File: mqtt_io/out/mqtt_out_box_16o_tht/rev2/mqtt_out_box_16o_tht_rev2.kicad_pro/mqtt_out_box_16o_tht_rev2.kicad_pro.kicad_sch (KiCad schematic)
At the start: 146 parts, among them J1 Conn_01x03_Pin, J2 Conn_01x03_Pin, Q1 IRFZ24N, SW1 SW_DIP_x03, U1 MCP23017_SP, U2 LF33_TO220

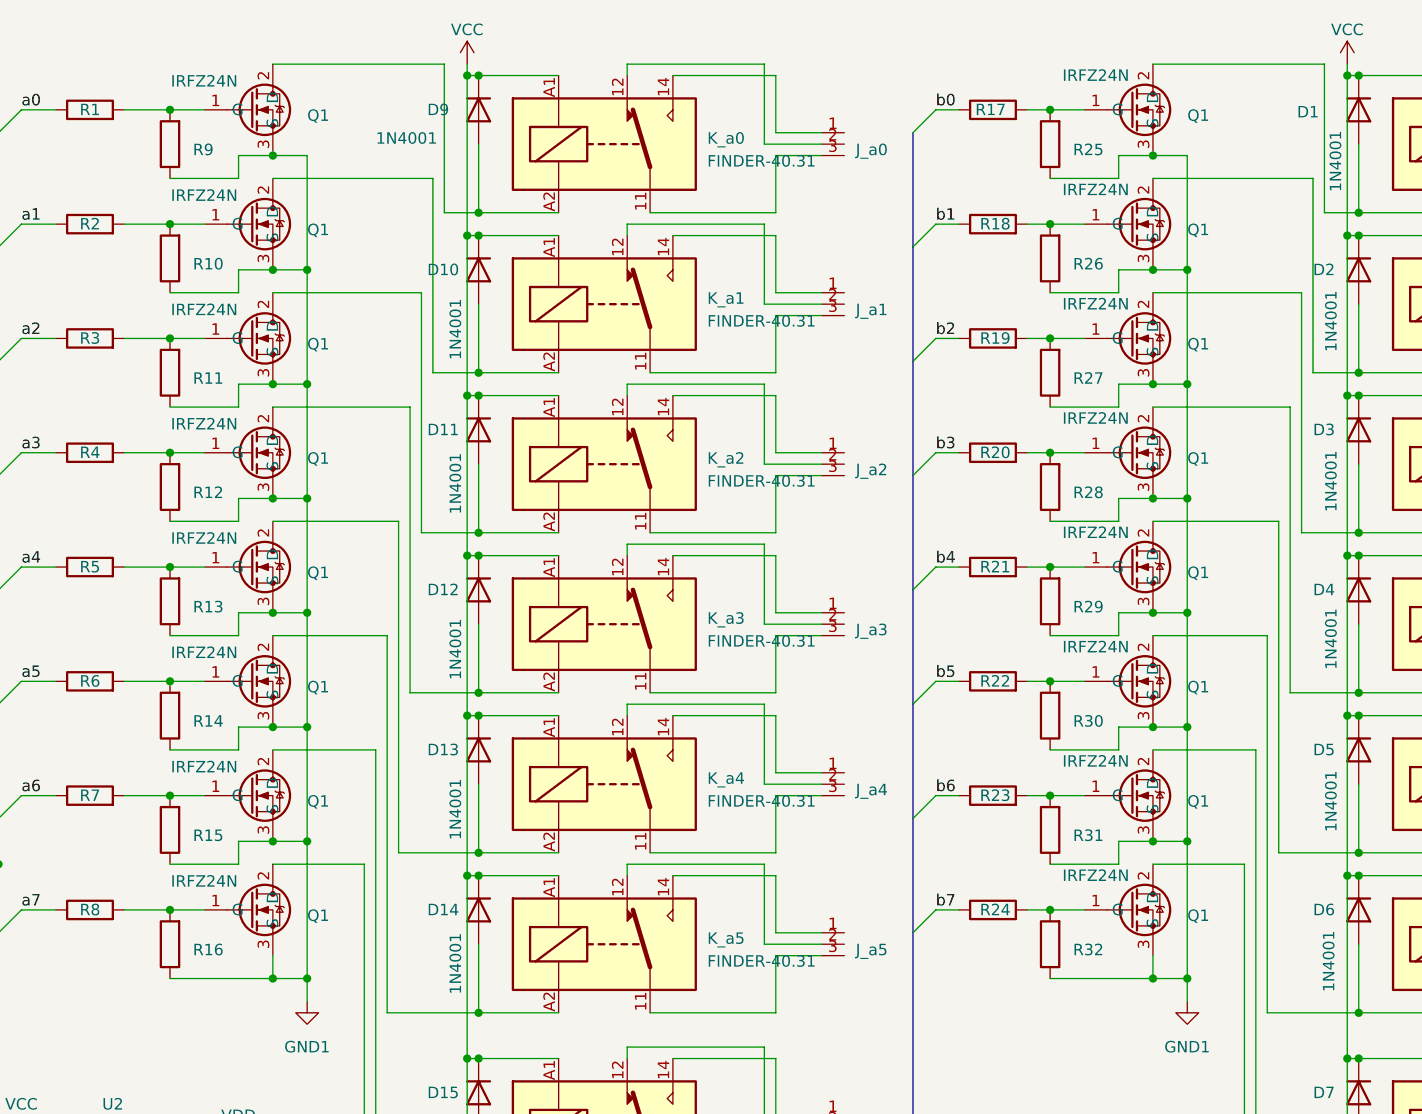
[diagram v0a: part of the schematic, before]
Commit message: umbau auf smd
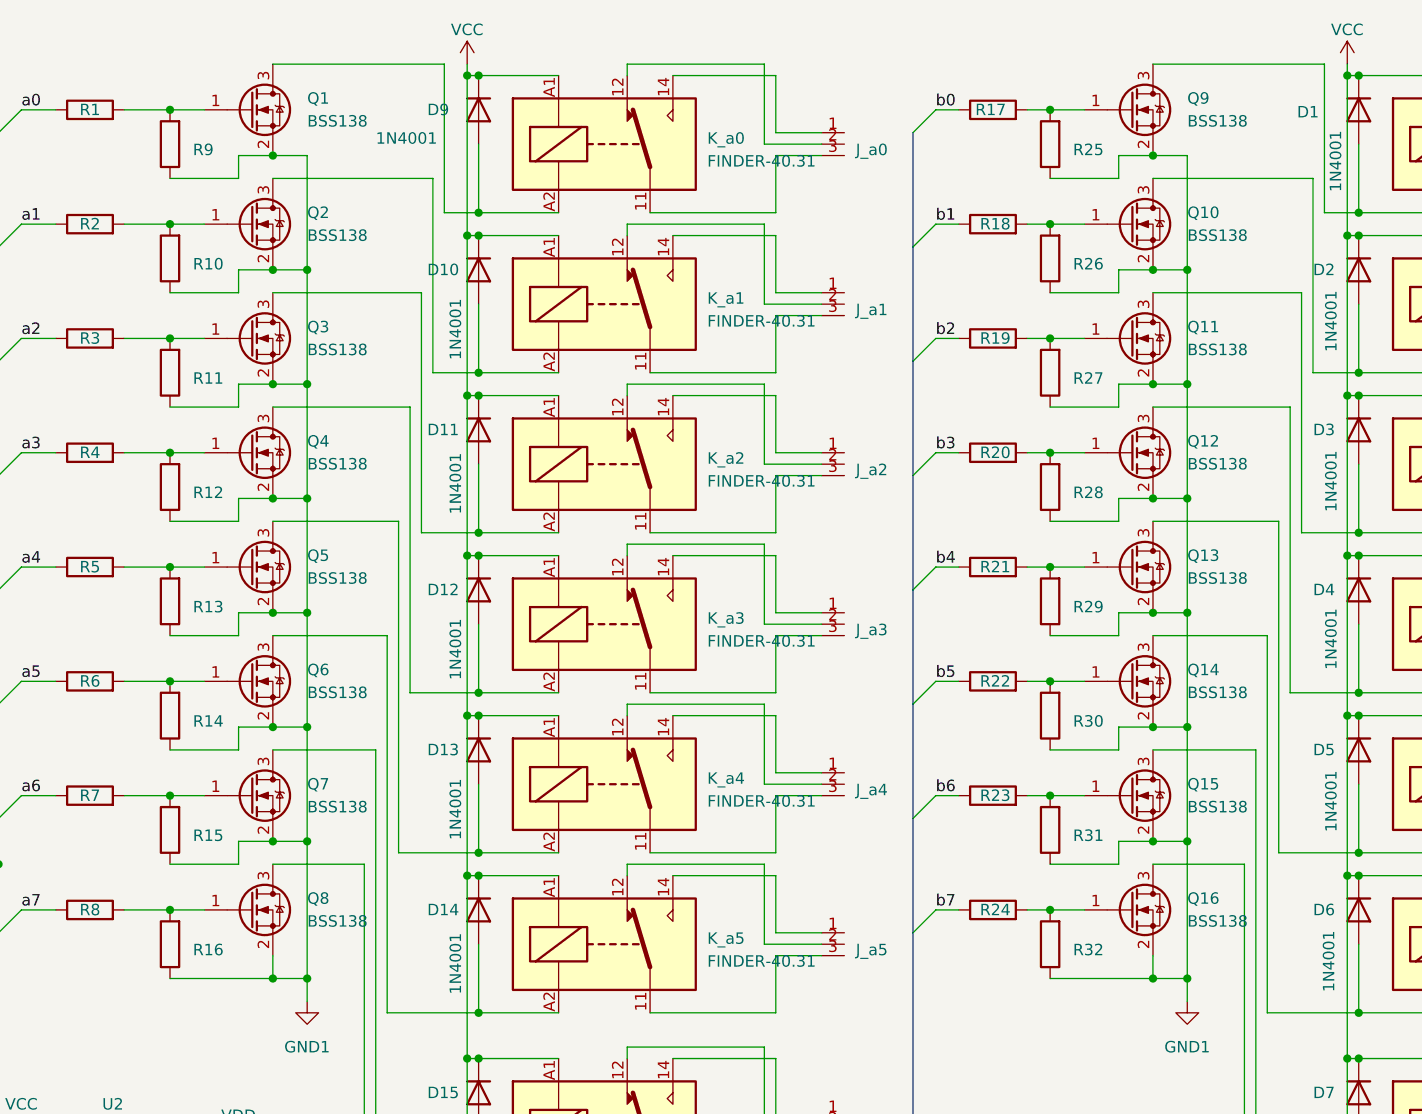
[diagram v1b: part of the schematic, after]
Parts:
- removed Q1 (x16): IRFZ24N, Package_TO_SOT_THT:TO-220-3_Vertical, symbol parts_tma_1:IRFZ_24N
- added Q1, Q10, Q11, Q12, Q13, Q14, Q15, Q16, Q2, Q3, Q4, Q5, Q6, Q7, Q8, Q9: BSS138, Package_TO_SOT_SMD:SOT-23, symbol Transistor_FET:BSS138
- C1: footprint Capacitor_THT:C_Rect_L4.6mm_W3.0mm_P2.50mm_MKS02_FKP02 -> Capacitor_SMD:C_0603_1608Metric_Pad1.08x0.95mm_HandSolder
- C2: footprint Capacitor_THT:C_Disc_D5.0mm_W2.5mm_P5.00mm -> Capacitor_SMD:C_0603_1608Metric_Pad1.08x0.95mm_HandSolder
- D1, D10, D11, D12, D13, D14, D15, D16, D2, D3, D4, D5, D6, D7, D8, D9: footprint Diode_THT:D_DO-41_SOD81_P10.16mm_Horizontal -> Diode_THT:D_A-405_P10.16mm_Horizontal
- D_a0, D_a1, D_a2, D_a3, D_a4, D_a5, D_a6, D_a7, D_b0, D_b1, D_b2, D_b3, D_b4, D_b5, D_b6, D_b7: footprint LED_THT:LED_D5.0mm -> LED_SMD:LED_0603_1608Metric_Pad1.05x0.95mm_HandSolder
- J1: footprint Connector_PinHeader_2.54mm:PinHeader_1x03_P2.54mm_Vertical -> Connector_PinHeader_2.54mm:PinHeader_1x03_P2.54mm_Horizontal
- J2: footprint Connector_PinHeader_2.54mm:PinHeader_1x03_P2.54mm_Vertical -> Connector_PinSocket_2.54mm:PinSocket_1x03_P2.54mm_Horizontal
- R1, R10, R11, R12, R13, R14, R15, R16, R17, R18, R19, R2, R20, R21, R22, R23, R24, R25, R26, R27, R28, R29, R3, R30, R31, R32, R33, R34, R35, R36, R37, R38, R39, R4, R40, R41, R42, R43, R44, R45, R46, R47, R48, R49, R5, R50, R51, R52, R53, R6, R7, R8, R9: footprint Resistor_THT:R_Axial_DIN0204_L3.6mm_D1.6mm_P7.62mm_Horizontal -> Resistor_SMD:R_0603_1608Metric_Pad0.98x0.95mm_HandSolder
- U1: footprint Package_DIP:DIP-28_W7.62mm -> Package_SO:SOIC-28W_7.5x18.7mm_P1.27mm
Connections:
- net GND: now also Q1.2 (S), Q10.2 (S), Q11.2 (S), Q12.2 (S), Q13.2 (S), Q14.2 (S), Q15.2 (S), Q16.2 (S), Q2.2 (S), Q3.2 (S), Q4.2 (S), Q5.2 (S), Q6.2 (S), Q7.2 (S), Q8.2 (S), Q9.2 (S)
- net at R17.2, R25.2: now also Q9.1 (G)
- net at D1.2 (A), K_b0.A2: now also Q9.3 (D)
- net at D12.2 (A), K_a3.A2: now also Q4.3 (D)
- net at R15.2, R7.2: now also Q7.1 (G)
- net at D15.2 (A), K_a6.A2: now also Q7.3 (D)
- net at R19.2, R27.2: now also Q11.1 (G)
- net at R24.2, R32.2: now also Q16.1 (G)
- net at R18.2, R26.2: now also Q10.1 (G)
- net at D2.2 (A), K_b1.A2: now also Q10.3 (D)
- net at D5.2 (A), K_b4.A2: now also Q13.3 (D)
- net at R10.2, R2.2: now also Q2.1 (G)
- net at D10.2 (A), K_a1.A2: now also Q2.3 (D)
- net at D13.2 (A), K_a4.A2: now also Q5.3 (D)
- net at D3.2 (A), K_b2.A2: now also Q11.3 (D)
- net at R12.2, R4.2: now also Q4.1 (G)
- net at R14.2, R6.2: now also Q6.1 (G)
- net at D14.2 (A), K_a5.A2: now also Q6.3 (D)
- net at R13.2, R5.2: now also Q5.1 (G)
- net at D7.2 (A), K_b6.A2: now also Q15.3 (D)
- net at D6.2 (A), K_b5.A2: now also Q14.3 (D)
- net at R22.2, R30.2: now also Q14.1 (G)
- net at R20.2, R28.2: now also Q12.1 (G)
- net at D9.2 (A), K_a0.A2: now also Q1.3 (D)
- net at R16.2, R8.2: now also Q8.1 (G)
- net at R11.2, R3.2: now also Q3.1 (G)
- net at D4.2 (A), K_b3.A2: now also Q12.3 (D)
- net at D16.2 (A), K_a7.A2: now also Q8.3 (D)
- net at D8.2 (A), K_b7.A2: now also Q16.3 (D)
- net at R1.2, R9.2: now also Q1.1 (G)
- net at R21.2, R29.2: now also Q13.1 (G)
- net at R23.2, R31.2: now also Q15.1 (G)
- net at D11.2 (A), K_a2.A2: now also Q3.3 (D)

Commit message: FET durch anderes Modell ersetzt
neu: 2N7000
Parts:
- removed Q1, Q10, Q11, Q12, Q13, Q14, Q15, Q16, Q2, Q3, Q4, Q5, Q6, Q7, Q8, Q9: BSS138, Package_TO_SOT_SMD:SOT-23, symbol Transistor_FET:BSS138
- added Q1, Q10, Q11, Q12, Q13, Q14, Q15, Q16, Q2, Q3, Q4, Q5, Q6, Q7, Q8, Q9: 2N7000, Package_TO_SOT_THT:TO-92_Inline, symbol Transistor_FET:2N7000
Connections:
- net GND: now also Q1.1 (S), Q10.1 (S), Q11.1 (S), Q12.1 (S), Q13.1 (S), Q14.1 (S), Q15.1 (S), Q16.1 (S), Q2.1 (S), Q3.1 (S), Q4.1 (S), Q5.1 (S), Q6.1 (S), Q7.1 (S), Q8.1 (S), Q9.1 (S)
- net at D12.2 (A), K_a3.A2: now also Q4.3 (D)
- net at R20.2, R28.2: now also Q11.2 (G)
- net at D4.2 (A), K_b3.A2: now also Q11.3 (D)
- net at R21.2, R29.2: now also Q10.2 (G)
- net at D5.2 (A), K_b4.A2: now also Q10.3 (D)
- net at R19.2, R27.2: now also Q12.2 (G)
- net at R17.2, R25.2: now also Q9.2 (G)
- net at D1.2 (A), K_b0.A2: now also Q9.3 (D)
- net at R10.2, R2.2: now also Q2.2 (G)
- net at D10.2 (A), K_a1.A2: now also Q2.3 (D)
- net at R24.2, R32.2: now also Q15.2 (G)
- net at D8.2 (A), K_b7.A2: now also Q15.3 (D)
- net at R1.2, R9.2: now also Q1.2 (G)
- net at D9.2 (A), K_a0.A2: now also Q1.3 (D)
- net at D13.2 (A), K_a4.A2: now also Q5.3 (D)
- net at R13.2, R5.2: now also Q5.2 (G)
- net at D15.2 (A), K_a6.A2: now also Q7.3 (D)
- net at D7.2 (A), K_b6.A2: now also Q14.3 (D)
- net at D6.2 (A), K_b5.A2: now also Q16.3 (D)
- net at R22.2, R30.2: now also Q16.2 (G)
- net at D2.2 (A), K_b1.A2: now also Q13.3 (D)
- net at R18.2, R26.2: now also Q13.2 (G)
- net at R14.2, R6.2: now also Q6.2 (G)
- net at R15.2, R7.2: now also Q7.2 (G)
- net at R16.2, R8.2: now also Q8.2 (G)
- net at R11.2, R3.2: now also Q3.2 (G)
- net at R12.2, R4.2: now also Q4.2 (G)
- net at D3.2 (A), K_b2.A2: now also Q12.3 (D)
- net at D14.2 (A), K_a5.A2: now also Q6.3 (D)
- net at D16.2 (A), K_a7.A2: now also Q8.3 (D)
- net at R23.2, R31.2: now also Q14.2 (G)
- net at D11.2 (A), K_a2.A2: now also Q3.3 (D)

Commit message: Platine geändert, BSS138
BSS138 SMD statt 2n7000 THT
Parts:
- removed Q1, Q10, Q11, Q12, Q13, Q14, Q15, Q16, Q2, Q3, Q4, Q5, Q6, Q7, Q8, Q9: 2N7000, Package_TO_SOT_THT:TO-92_Inline, symbol Transistor_FET:2N7000
- added Q1, Q10, Q11, Q12, Q13, Q14, Q15, Q16, Q2, Q3, Q4, Q5, Q6, Q7, Q8, Q9: BSS138, Package_TO_SOT_SMD:SOT-23, symbol Transistor_FET:BSS138
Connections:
- net GND: now also Q1.2 (S), Q10.2 (S), Q11.2 (S), Q12.2 (S), Q13.2 (S), Q14.2 (S), Q15.2 (S), Q16.2 (S), Q2.2 (S), Q3.2 (S), Q4.2 (S), Q5.2 (S), Q6.2 (S), Q7.2 (S), Q8.2 (S), Q9.2 (S)
- net at R10.2, R2.2: now also Q2.1 (G)
- net at D10.2 (A), K_a1.A2: now also Q2.3 (D)
- net at D12.2 (A), K_a3.A2: now also Q4.3 (D)
- net at R17.2, R25.2: now also Q9.1 (G)
- net at D1.2 (A), K_b0.A2: now also Q9.3 (D)
- net at R19.2, R27.2: now also Q11.1 (G)
- net at R24.2, R32.2: now also Q16.1 (G)
- net at D8.2 (A), K_b7.A2: now also Q16.3 (D)
- net at R1.2, R9.2: now also Q1.1 (G)
- net at D9.2 (A), K_a0.A2: now also Q1.3 (D)
- net at R23.2, R31.2: now also Q15.1 (G)
- net at D7.2 (A), K_b6.A2: now also Q15.3 (D)
- net at D5.2 (A), K_b4.A2: now also Q13.3 (D)
- net at R21.2, R29.2: now also Q13.1 (G)
- net at D13.2 (A), K_a4.A2: now also Q5.3 (D)
- net at R14.2, R6.2: now also Q6.1 (G)
- net at D14.2 (A), K_a5.A2: now also Q6.3 (D)
- net at R13.2, R5.2: now also Q5.1 (G)
- net at D15.2 (A), K_a6.A2: now also Q7.3 (D)
- net at D6.2 (A), K_b5.A2: now also Q14.3 (D)
- net at R22.2, R30.2: now also Q14.1 (G)
- net at R20.2, R28.2: now also Q12.1 (G)
- net at D2.2 (A), K_b1.A2: now also Q10.3 (D)
- net at R18.2, R26.2: now also Q10.1 (G)
- net at R16.2, R8.2: now also Q8.1 (G)
- net at R11.2, R3.2: now also Q3.1 (G)
- net at R12.2, R4.2: now also Q4.1 (G)
- net at D3.2 (A), K_b2.A2: now also Q11.3 (D)
- net at D16.2 (A), K_a7.A2: now also Q8.3 (D)
- net at R15.2, R7.2: now also Q7.1 (G)
- net at D4.2 (A), K_b3.A2: now also Q12.3 (D)
- net at D11.2 (A), K_a2.A2: now also Q3.3 (D)
